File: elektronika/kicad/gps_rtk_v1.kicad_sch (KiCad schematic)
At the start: 0 parts

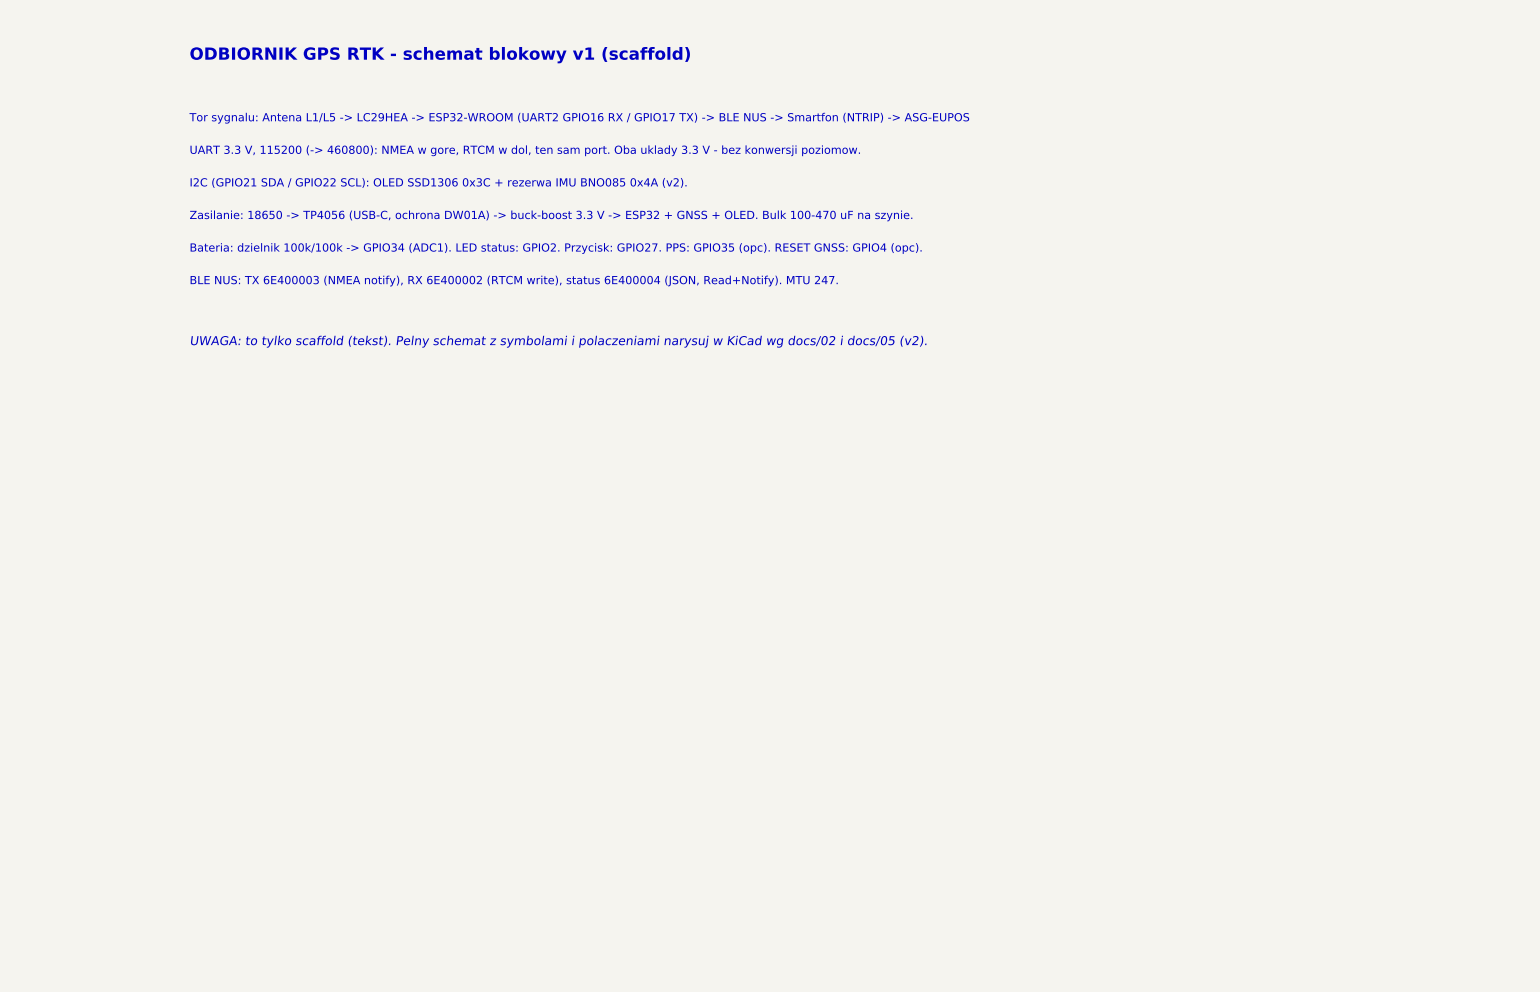
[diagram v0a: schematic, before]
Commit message: elektronika/kicad: schemat blokowy + eksport PDF/SVG (kicad-cli 9.0.9)
- gps_rtk_v1.kicad_sch: scaffold -> natywny schemat blokowy (bloki + polaczenia + etykiety netow)
- zwalidowany i wyrenderowany kicad-cli 9.0.9 -> gps_rtk_v1.pdf + gps_rtk_v1.svg
- README: portable KiCad (rozpakowany 7-Zipem, GUI+CLI) + instrukcje

Co-Authored-By: Claude Opus 4.8 (1M context) <noreply@anthropic.com>
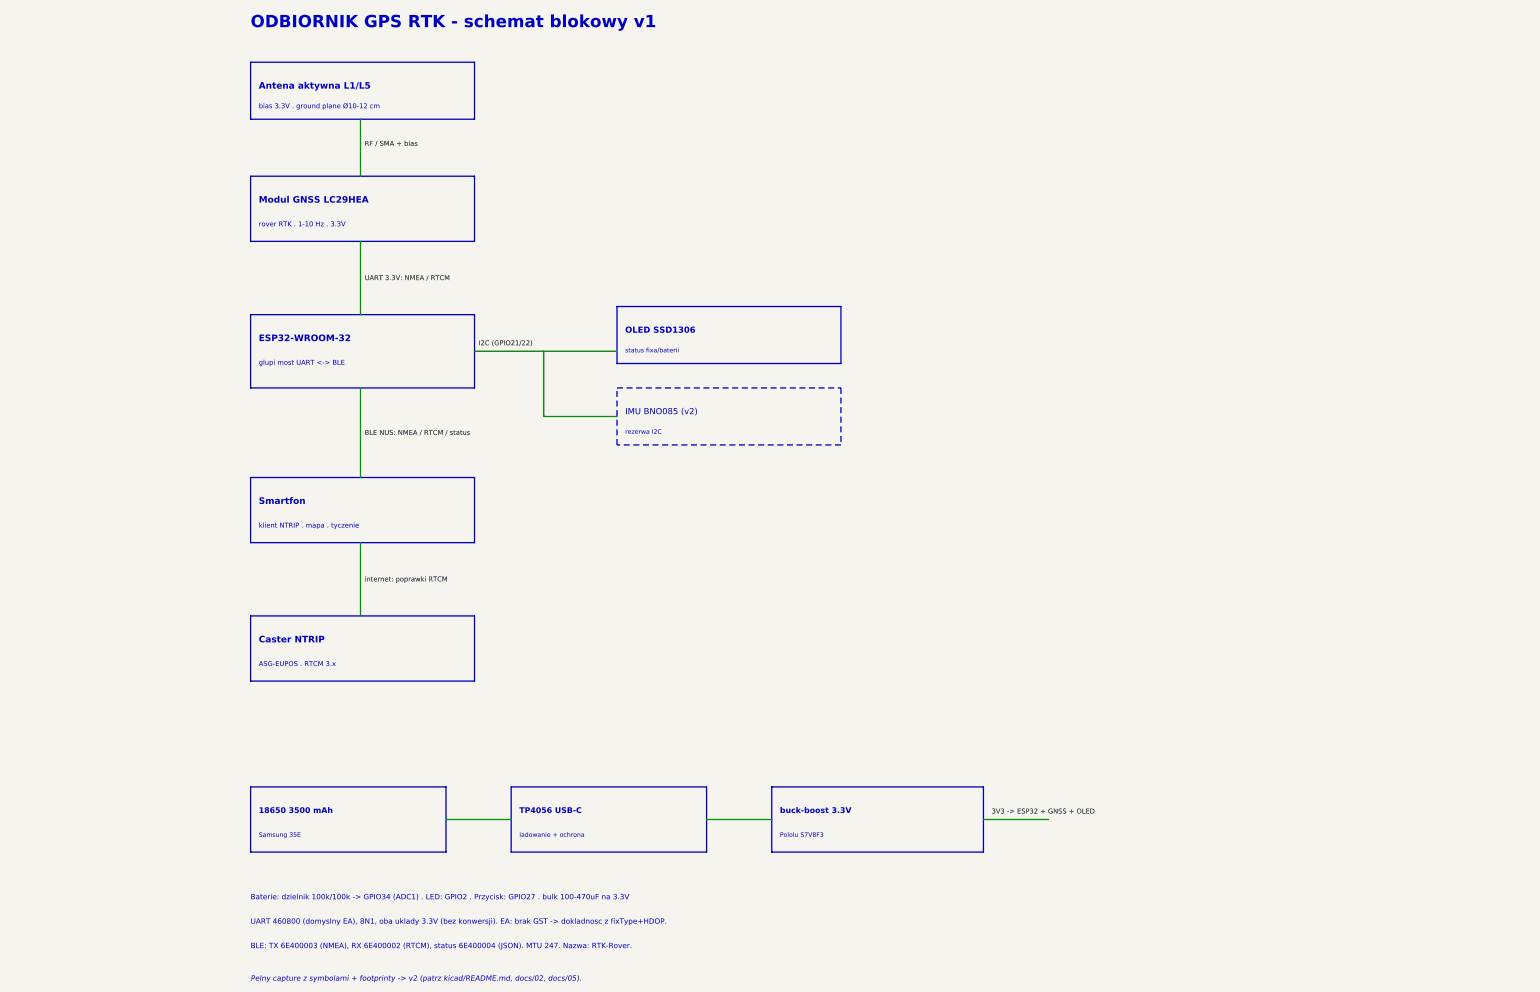
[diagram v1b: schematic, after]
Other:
- note added: "18650 3500 mAh"
- note added: "ASG-EUPOS . RTCM 3.x"
- note added: "Antena aktywna L1/L5"
- note added: "BLE: TX 6E400003 (NMEA), RX 6E400002 (RTCM), status 6E400004 (JSON). MTU 247. Nazwa: RTK-Rover."
- note added: "Baterie: dzielnik 100k/100k -> GPIO34 (ADC1) . LED: GPIO2 . Przycisk: GPIO27 . bulk 100-470uF na 3.3V"
- note added: "Caster NTRIP"
- note added: "ESP32-WROOM-32"
- note added: "IMU BNO085 (v2)"
- note added: "Modul GNSS LC29HEA"
- note added: "ODBIORNIK GPS RTK - schemat blokowy v1"
- note added: "OLED SSD1306"
- note added: "Pelny capture z symbolami + footprinty -> v2 (patrz kicad/README.md, docs/02, docs/05)."
- note added: "Pololu S7V8F3"
- note added: "Samsung 35E"
- note added: "Smartfon"
- note added: "TP4056 USB-C"
- note added: "UART 460800 (domyslny EA), 8N1, oba uklady 3.3V (bez konwersji). EA: brak GST -> dokladnosc z fixType+HDOP."
- note added: "bias 3.3V . ground plane Ø10-12 cm"
- note added: "buck-boost 3.3V"
- note added: "glupi most UART <-> BLE"
- note added: "klient NTRIP . mapa . tyczenie"
- note added: "ladowanie + ochrona"
- note added: "rezerwa I2C"
- note added: "rover RTK . 1-10 Hz . 3.3V"
- note added: "status fixa/baterii"
- note removed: "BLE NUS: TX 6E400003 (NMEA notify), RX 6E400002 (RTCM write), status 6E400004 (JSON, Read+Notify). MTU 247."
- note removed: "Bateria: dzielnik 100k/100k -> GPIO34 (ADC1). LED status: GPIO2. Przycisk: GPIO27. PPS: GPIO35 (opc). RESET GNSS: GPIO4 (opc)."
- note removed: "I2C (GPIO21 SDA / GPIO22 SCL): OLED SSD1306 0x3C + rezerwa IMU BNO085 0x4A (v2)."
- note removed: "ODBIORNIK GPS RTK - schemat blokowy v1 (scaffold)"
- note removed: "Tor sygnalu: Antena L1/L5 -> LC29HEA -> ESP32-WROOM (UART2 GPIO16 RX / GPIO17 TX) -> BLE NUS -> Smartfon (NTRIP) -> ASG-EUPOS"
- note removed: "UART 3.3 V, 115200 (-> 460800): NMEA w gore, RTCM w dol, ten sam port. Oba uklady 3.3 V - bez konwersji poziomow."
- note removed: "UWAGA: to tylko scaffold (tekst). Pelny schemat z symbolami i polaczeniami narysuj w KiCad wg docs/02 i docs/05 (v2)."
- note removed: "Zasilanie: 18650 -> TP4056 (USB-C, ochrona DW01A) -> buck-boost 3.3 V -> ESP32 + GNSS + OLED. Bulk 100-470 uF na szynie."
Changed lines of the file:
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@@
 		(rev "v1")
 		(company "Projekt GPS_RTK")
-		(comment 1 "Scaffold - uzupelnic symbolami w KiCad (v2)")
+		(comment 1 "Schemat blokowy - capture z symbolami w v2")
 		(comment 2 "Polaczenia: elektronika/docs/02-schemat-polaczen.md")
 		(comment 3 "Pinout/protokol BLE: elektronika/docs/05-pinout-firmware.md")
 	)
-	(text "ODBIORNIK GPS RTK - schemat blokowy v1 (scaffold)"
+	(text "ODBIORNIK GPS RTK - schemat blokowy v1"
 		(exclude_from_sim no)
-		(at 25 30 0)
-		(effects
-			(font (size 3 3) (bold yes))
-			(justify left bottom)
-		)
+		(at 40 22 0)
+		(effects (font (size 3 3) (bold yes)) (justify left bottom))
 	)
-	(text "Tor sygnalu: Antena L1/L5 -> LC29HEA -> ESP32-WROOM (UART2 GPIO16 RX / GPIO17 TX) -> BLE NUS -> Smartfon (NTRIP) -> ASG-EUPOS"
-		(exclude_from_sim no)
-		(at 25 45 0)
-		(effects
-			(font (size 2 2))
-			(justify left bottom)
-		)
-	)
-	(text "UART 3.3 V, 115200 (-> 460800): NMEA w gore, RTCM w dol, ten sam port. Oba uklady 3.3 V - bez konwersji poziomow."
-		(exclude_from_sim no)
-		(at 25 53 0)
-		(effects
-			(font (size 2 2))
-			(justify left bottom)
-		)
-	)
-	(text "I2C (GPIO21 SDA / GPIO22 SCL): OLED SSD1306 0x3C + rezerwa IMU BNO085 0x4A (v2)."
-		(exclude_from_sim no)
-		(at 25 61 0)
-		(effects
-			(font (size 2 2))
-			(justify left bottom)
-		)
-	)
-	(text "Zasilanie: 18650 -> TP4056 (USB-C, ochrona DW01A) -> buck-boost 3.3 V -> ESP32 + GNSS + OLED. Bulk 100-470 uF na szynie."
-		(exclude_from_sim no)
-		(at 25 69 0)
-		(effects
-			(font (size 2 2))
-			(justify left bottom)
-		)
-	)
-	(text "Bateria: dzielnik 100k/100k -> GPIO34 (ADC1). LED status: GPIO2. Przycisk: GPIO27. PPS: GPIO35 (opc). RESET GNSS: GPIO4 (opc)."
-		(exclude_from_sim no)
-		(at 25 77 0)
-		(effects
-			(font (size 2 2))
-			(justify left bottom)
-		)
-	)
-	(text "BLE NUS: TX 6E400003 (NMEA notify), RX 6E400002 (RTCM write), status 6E400004 (JSON, Read+Notify). MTU 247."
-		(exclude_from_sim no)
-		(at 25 85 0)
-		(effects
-			(font (size 2 2))
-			(justify left bottom)
-		)
-	)
-	(text "UWAGA: to tylko scaffold (tekst). Pelny schemat z symbolami i polaczeniami narysuj w KiCad wg docs/02 i docs/05 (v2)."
-		(exclude_from_sim no)
-		(at 25 100 0)
-		(effects
-			(font (size 2.2 2.2) (italic yes))
-			(justify left bottom)
-		)
-	)
+	(rectangle (start 40 30) (end 95 44)
+		(stroke (width 0.3) (type default)) (fill (type none))
+)
+	(text "Antena aktywna L1/L5"
+		(exclude_from_sim no) (at 42 36 0)
+		(effects (font (size 1.6 1.6) (bold yes)) (justify left))
+)
+	(text "bias 3.3V . ground plane Ø10-12 cm"
+		(exclude_from_sim no) (at 42 41 0)
+		(effects (font (size 1.2 1.2)) (justify left))
+)
+	(rectangle (start 40 58) (end 95 74)
+		(stroke (width 0.3) (type default)) (fill (type none))
+)
+	(text "Modul GNSS LC29HEA"
+		(exclude_from_sim no) (at 42 64 0)
+		(effects (font (size 1.6 1.6) (bold yes)) (justify left))
+)
+	(text "rover RTK . 1-10 Hz . 3.3V"
+		(exclude_from_sim no) (at 42 70 0)
+		(effects (font (size 1.2 1.2)) (justify left))
+)
+	(rectangle (start 40 92) (end 95 110)
+		(stroke (width 0.3) (type default)) (fill (type none))
+)
+	(text "ESP32-WROOM-32"
+		(exclude_from_sim no) (at 42 98 0)
+		(effects (font (size 1.6 1.6) (bold yes)) (justify left))
+)
+	(text "glupi most UART <-> BLE"
+		(exclude_from_sim no) (at 42 104 0)
+		(effects (font (size 1.2 1.2)) (justify left))
+)
+	(rectangle (start 40 132) (end 95 148)
+		(stroke (width 0.3) (type default)) (fill (type none))
+)
+	(text "Smartfon"
+		(exclude_from_sim no) (at 42 138 0)
+		(effects (font (size 1.6 1.6) (bold yes)) (justify left))
+)
+	(text "klient NTRIP . mapa . tyczenie"
+		(exclude_from_sim no) (at 42 144 0)
+		(effects (font (size 1.2 1.2)) (justify left))
+)
+	(rectangle (start 40 166) (end 95 182)
+		(stroke (width 0.3) (type default)) (fill (type none))
+)
+	(text "Caster NTRIP"
+		(exclude_from_sim no) (at 42 172 0)
+		(effects (font (size 1.6 1.6) (bold yes)) (justify left))
+)
+	(text "ASG-EUPOS . RTCM 3.x"
+		(exclude_from_sim no) (at 42 178 0)
+		(effects (font (size 1.2 1.2)) (justify left))
+)
+	(rectangle (start 130 90) (end 185 104)
+		(stroke (width 0.3) (type default)) (fill (type none))
+)
+	(text "OLED SSD1306"
+		(exclude_from_sim no) (at 132 96 0)
+		(effects (font (size 1.5 1.5) (bold yes)) (justify left))
+)
+	(text "status fixa/baterii"
+		(exclude_from_sim no) (at 132 101 0)
+		(effects (font (size 1.1 1.1)) (justify left))
+)
+	(rectangle (start 130 110) (end 185 124)
+		(stroke (width 0.2) (type dash)) (fill (type none))
+)
+	(text "IMU BNO085 (v2)"
+		(exclude_from_sim no) (at 132 116 0)
+		(effects (font (size 1.5 1.5)) (justify left))
+)
+	(text "rezerwa I2C"
+		(exclude_from_sim no) (at 132 121 0)
+		(effects (font (size 1.1 1.1)) (justify left))
+)
+	(rectangle (start 40 208) (end 88 224)
+		(stroke (width 0.3) (type default)) (fill (type none))
+)
+	(text "18650 3500 mAh"
+		(exclude_from_sim no) (at 42 214 0)
+		(effects (font (size 1.4 1.4) (bold yes)) (justify left))
+)
+	(text "Samsung 35E"
+		(exclude_from_sim no) (at 42 220 0)
+		(effects (font (size 1.1 1.1)) (justify left))
+)
+	(rectangle (start 104 208) (end 152 224)
+		(stroke (width 0.3) (type default)) (fill (type none))
+)
+	(text "TP4056 USB-C"
+		(exclude_from_sim no) (at 106 214 0)
+		(effects (font (size 1.4 1.4) (bold yes)) (justify left))
+)
+	(text "ladowanie + ochrona"
+		(exclude_from_sim no) (at 106 220 0)
+		(effects (font (size 1.1 1.1)) (justify left))
+)
+	(rectangle (start 168 208) (end 220 224)
+		(stroke (width 0.3) (type default)) (fill (type none))
+)
+	(text "buck-boost 3.3V"
+		(exclude_from_sim no) (at 170 214 0)
+		(effects (font (size 1.4 1.4) (bold yes)) (justify left))
+)
+	(text "Pololu S7V8F3"
+		(exclude_from_sim no) (at 170 220 0)
+		(effects (font (size 1.1 1.1)) (justify left))
+)
+	(wire (pts (xy 67 44) (xy 67 58)) (stroke (width 0.2) (type default))
+)
+	(label "RF / SMA + bias" (at 68 51 0)
+		(effects (font (size 1.2 1.2)) (justify left bottom))
+)
+	(wire (pts (xy 67 74) (xy 67 92)) (stroke (width 0.2) (type default))
+)
+	(label "UART 3.3V: NMEA / RTCM" (at 68 84 0)
+		(effects (font (size 1.2 1.2)) (justify left bottom))
+)
+	(wire (pts (xy 67 110) (xy 67 132)) (stroke (width 0.2) (type default))
+)
+	(label "BLE NUS: NMEA / RTCM / status" (at 68 122 0)
+		(effects (font (size 1.2 1.2)) (justify left bottom))
+)
+	(wire (pts (xy 67 148) (xy 67 166)) (stroke (width 0.2) (type default))
+)
+	(label "internet: poprawki RTCM" (at 68 158 0)
+		(effects (font (size 1.2 1.2)) (justify left bottom))
+)
+	(wire (pts (xy 95 101) (xy 130 101)) (stroke (width 0.2) (type default))
+)
+	(wire (pts (xy 112 101) (xy 112 117)) (stroke (width 0.2) (type default))
+)
+	(wire (pts (xy 112 117) (xy 130 117)) (stroke (width 0.2) (type default))
+)
+	(label "I2C (GPIO21/22)" (at 96 100 0)
+		(effects (font (size 1.2 1.2)) (justify left bottom))
+)
+	(wire (pts (xy 88 216) (xy 104 216)) (stroke (width 0.2) (type default))
+)
+	(wire (pts (xy 152 216) (xy 168 216)) (stroke (width 0.2) (type default))
+)
+	(wire (pts (xy 220 216) (xy 236 216)) (stroke (width 0.2) (type default))
+)
+	(label "3V3 -> ESP32 + GNSS + OLED" (at 222 215 0)
+		(effects (font (size 1.2 1.2)) (justify left bottom))
+)
+	(text "Baterie: dzielnik 100k/100k -> GPIO34 (ADC1) . LED: GPIO2 . Przycisk: GPIO27 . bulk 100-470uF na 3.3V"
+		(exclude_from_sim no) (at 40 236 0)
+		(effects (font (size 1.3 1.3)) (justify left bottom))
+)
+	(text "UART 460800 (domyslny EA), 8N1, oba uklady 3.3V (bez konwersji). EA: brak GST -> dokladnosc z fixType+HDOP."
+		(exclude_from_sim no) (at 40 242 0)
+		(effects (font (size 1.3 1.3)) (justify left bottom))
+)
+	(text "BLE: TX 6E400003 (NMEA), RX 6E400002 (RTCM), status 6E400004 (JSON). MTU 247. Nazwa: RTK-Rover."
+		(exclude_from_sim no) (at 40 248 0)
+		(effects (font (size 1.3 1.3)) (justify left bottom))
+)
+	(text "Pelny capture z symbolami + footprinty -> v2 (patrz kicad/README.md, docs/02, docs/05)."
+		(exclude_from_sim no) (at 40 256 0)
+		(effects (font (size 1.3 1.3) (italic yes)) (justify left bottom))
+)
 	(sheet_instances
-		(path "/"
-			(page "1")
-		)
+		(path "/" (page "1"))
 	)
 )
